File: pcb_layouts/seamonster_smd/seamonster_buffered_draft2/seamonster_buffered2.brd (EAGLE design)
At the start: 172.5 x 106.5 mm, 132 parts, among them IC1 7808DT, IC2 4051D, IC3 4051D, IC4 DG408DY, IC5 4046D, IC6 40106D, IC7 4070D, IC8 4046D, IC9 4040D, Q1 THONKICONNNEW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

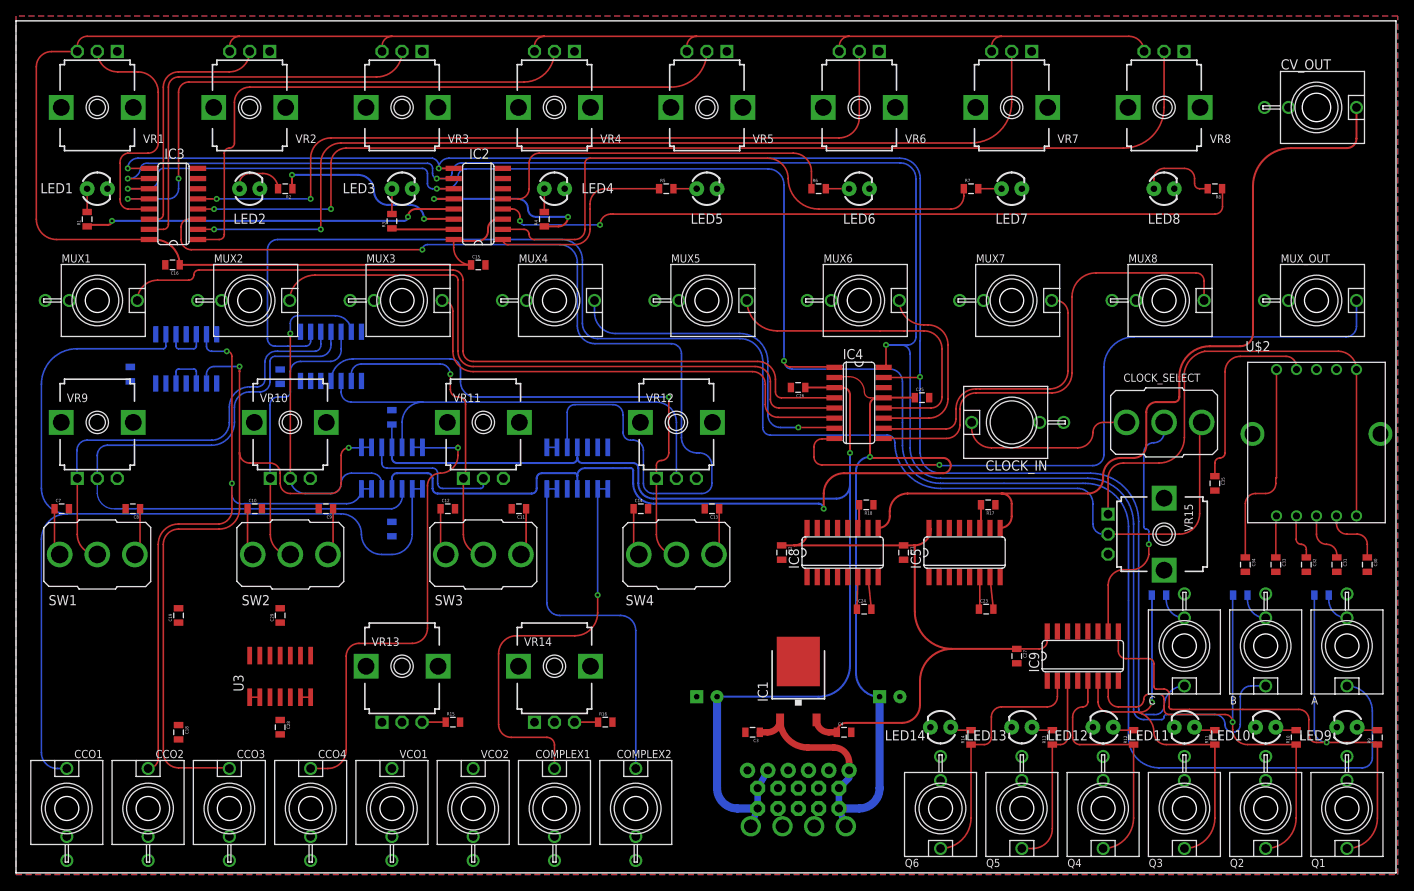
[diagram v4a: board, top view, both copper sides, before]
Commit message: connected power nets up, moved and routed VCOs
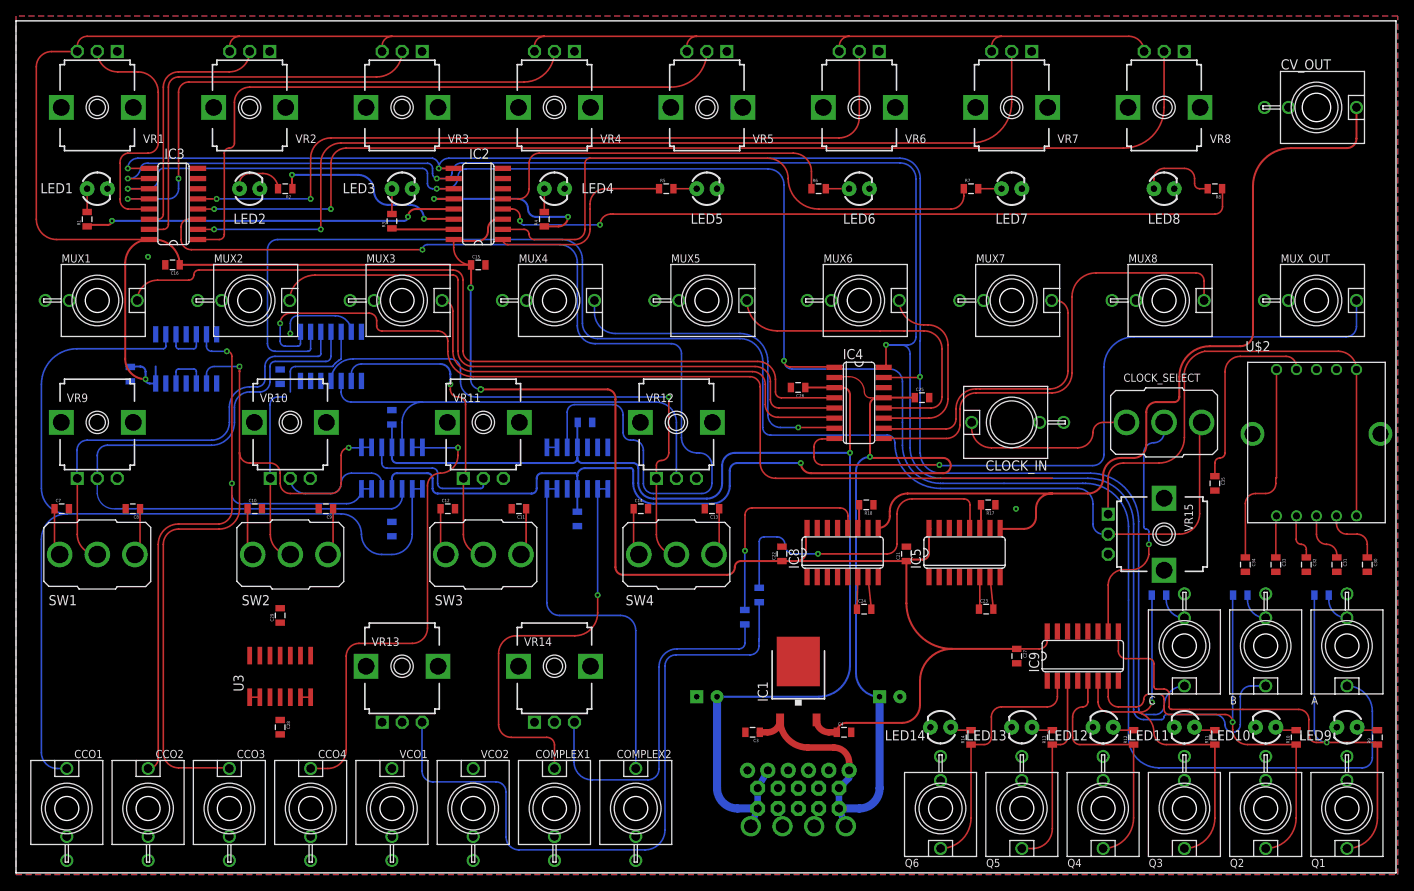
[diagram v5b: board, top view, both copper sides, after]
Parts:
- moved C18 56.5 mm to (70.2, 55.2), flipped to the bottom
- moved C19 56.2 mm to (71.1, 67.3), flipped to the bottom, turned to 180 degrees
- moved R15 41.5 mm to (92.9, 45.7), flipped to the bottom, turned to 90 degrees
- moved R16 21.8 mm to (91.1, 43.0), flipped to the bottom, turned to 90 degrees
- moved C21 0.39 mm to (111.3, 50.9), turned to 90 degrees
- moved C22 0.17 mm to (95.7, 50.9), turned to 90 degrees
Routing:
- net N$2: track 65.9 -> 184.8 mm, vias 0 -> 1
- net VCC: track 317.6 -> 423.3 mm, vias 0 -> 3
- net N$42: track 2.96 -> 83.9 mm
- net N$40: track 0.00 -> 41.5 mm, vias 0 -> 1
- net N$72: track 2.96 -> 44.4 mm
- net N$71: track 0.00 -> 27.1 mm, vias 0 -> 1
- net INV_C_OUT: track 42.7 -> 24.6 mm
- net V-: track 151.5 -> 157.6 mm
- net CV_OUT_BUFFERED: track 105.8 -> 109.3 mm
- net V+: track 185.2 -> 188.6 mm
- net N$43: track 174.2 -> 175.7 mm

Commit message: added to-do text file for PCB revisions
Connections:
- new net N$9: MUX_OUT.P$1_TIP, U2.13, U2.14
- net N$1: now also U2.12; no longer MUX_OUT.P$1_TIP
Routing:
- net N$1: track 89.4 -> 0.00 mm, vias 1 -> 0
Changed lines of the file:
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@@
 <wire x1="140.335" y1="54.9275" x2="140.335" y2="31.4325" width="0.2032" layer="16"/>
-</signal>
-<signal name="N$1">
-<contactref element="IC4" pad="8"/>
-<contactref element="MUX_OUT" pad="P$1_TIP"/>
-<wire x1="102.3066" y1="65.305" x2="102.2516" y2="65.25" width="0.2032" layer="1" curve="-90"/>
-<wire x1="102.2516" y1="65.25" x2="100.75" y2="65.25" width="0.2032" layer="1"/>
-<wire x1="100.75" y1="65.25" x2="99.75" y2="64.25" width="0.2032" layer="1" curve="90"/>
-<wire x1="99.75" y1="64.25" x2="99.75" y2="63" width="0.2032" layer="1"/>
-<wire x1="99.75" y1="63" x2="100.75" y2="62" width="0.2032" layer="1" curve="90"/>
-<via x="115.4225" y="62" extent="1-16" drill="0.35"/>
-<wire x1="136" y1="74.25" x2="139.75" y2="78" width="0.2032" layer="16" curve="-90"/>
-<wire x1="166.25" y1="78" x2="167.56" y2="79.31" width="0.2032" layer="16" curve="90"/>
-<wire x1="167.56" y1="79.31" x2="167.56" y2="82.55" width="0.2032" layer="16"/>
-<wire x1="100.75" y1="62" x2="115.4225" y2="62" width="0.2032" layer="1"/>
-<wire x1="139.75" y1="78" x2="166.25" y2="78" width="0.2032" layer="16"/>
-<wire x1="115.4225" y1="62" x2="115.51" y2="61.9125" width="0.2032" layer="16" curve="90"/>
-<wire x1="134.62" y1="61.9125" x2="136" y2="63.2925" width="0.2032" layer="16" curve="90"/>
-<wire x1="115.51" y1="61.9125" x2="134.62" y2="61.9125" width="0.2032" layer="16"/>
-<wire x1="136" y1="63.2925" x2="136" y2="74.25" width="0.2032" layer="16"/>
 </signal>
 <signal name="N$10">
@@
 <wire x1="153.035" y1="75.565" x2="158.75" y2="75.565" width="0.2032" layer="1"/>
 </signal>
+<signal name="N$1">
+<contactref element="IC4" pad="8"/>
+<contactref element="U2" pad="12"/>
+<wire x1="71.4375" y1="64.195" x2="102.3066" y2="65.305" width="0" layer="19" extent="1-16"/>
+</signal>
+<signal name="N$9">
+<contactref element="U2" pad="13"/>
+<contactref element="U2" pad="14"/>
+<contactref element="MUX_OUT" pad="P$1_TIP"/>
+<wire x1="73.9775" y1="64.195" x2="167.56" y2="82.55" width="0" layer="19" extent="16-16"/>
+<wire x1="72.7075" y1="64.195" x2="73.9775" y2="64.195" width="0" layer="19" extent="16-16"/>
+</signal>
 </signals>

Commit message: finished routing, working on silkscreen
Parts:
- moved C17 2.03 mm to (33.0, 75.1), flipped to the top
- moved C5 2.00 mm to (47.0, 56.0)
- moved C30 1.14 mm to (167.9, 49.0)
- moved C31 1.14 mm to (164.1, 49.0)
- moved C32 1.14 mm to (160.3, 49.0)
- moved C33 1.14 mm to (156.5, 49.0)
- moved C34 1.14 mm to (152.7, 49.0)
- moved U$2 1.14 mm to (161.5, 64.3)
- moved C20 0.71 mm to (14.8, 72.8)
- moved C19 0.50 mm to (71.1, 67.8)
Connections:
- removed net N$73: CCO1.P$3_SLEEVE, CCO2.P$3_SLEEVE, CCO3.P$3_SLEEVE, CCO4.P$3_SLEEVE, COMPLEX1.P$3_SLEEVE, COMPLEX2.P$3_SLEEVE
- net GND: now also CCO1.P$3_SLEEVE, CCO2.P$3_SLEEVE, CCO3.P$3_SLEEVE, CCO4.P$3_SLEEVE, COMPLEX1.P$3_SLEEVE, COMPLEX2.P$3_SLEEVE
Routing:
- net N$9: track 0.00 -> 171.8 mm, vias 0 -> 3
- net N$39: track 0.00 -> 161.0 mm, vias 0 -> 2
- net VCO1_OUT: track 0.00 -> 126.2 mm
- net VCO2_OUT_BUFFERED: track 1.27 -> 105.8 mm, vias 0 -> 5
- net N$38: track 0.00 -> 81.6 mm, vias 0 -> 2
- net VCO2_OUT: track 0.00 -> 76.5 mm, vias 0 -> 2
- net CV_OUT_BUFFERED: track 109.3 -> 173.6 mm, vias 0 -> 1
- net CCO4_BUFFERED: track 59.2 -> 107.4 mm, vias 1 -> 3
- net V-: track 157.6 -> 202.2 mm, vias 1 -> 2
- net N$1: track 0.00 -> 44.6 mm, vias 0 -> 3
- net V+: track 188.6 -> 227.2 mm, vias 2 -> 3
- net VCC: track 423.3 -> 457.4 mm, vias 3 -> 4
- net INV_C_OUT: track 24.6 -> 50.3 mm, vias 1 -> 3
- net VCO1_OUT_BUFFERED: track 1.27 -> 23.8 mm, vias 0 -> 1
- net N$2: track 184.8 -> 199.6 mm, vias 1 -> 3
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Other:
- board size 172.5 x 106.5 mm -> 172.5 x 106.7 mm
- board text added: "SeaMonster"
- board text added: "revision 1.0 designed by Shaurjya Banerjee june 2018"
